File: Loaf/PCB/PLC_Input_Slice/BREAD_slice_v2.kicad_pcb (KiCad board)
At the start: 2 copper layers, 100 x 70.6 mm, 31 parts, among them J1 10018783-10200TLF, J2 Barrel_Jack, J3 DB25_Socket, U1 MCP4922-EP, U2 MCP4922-EP, U3 MCP4922-EP, U4 MCP4922-EP, U5 MCP3208, U6 MCP2561-E-P, U7 MCP2515-xSO, Y1 16MHZ Crystal

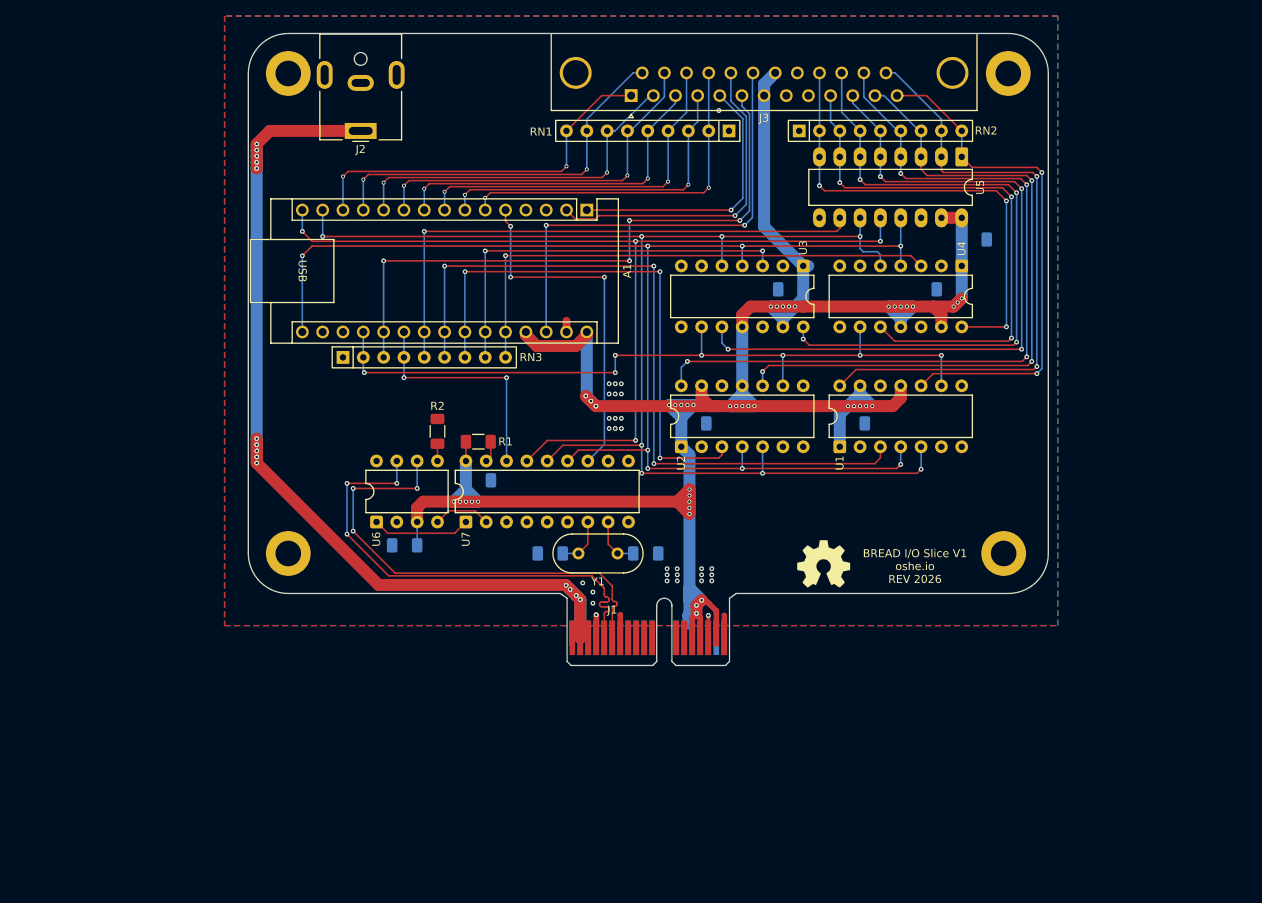
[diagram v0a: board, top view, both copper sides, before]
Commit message: IO PCB redesign progress upload
Switching to pi pico for better performance and to keep UART interface
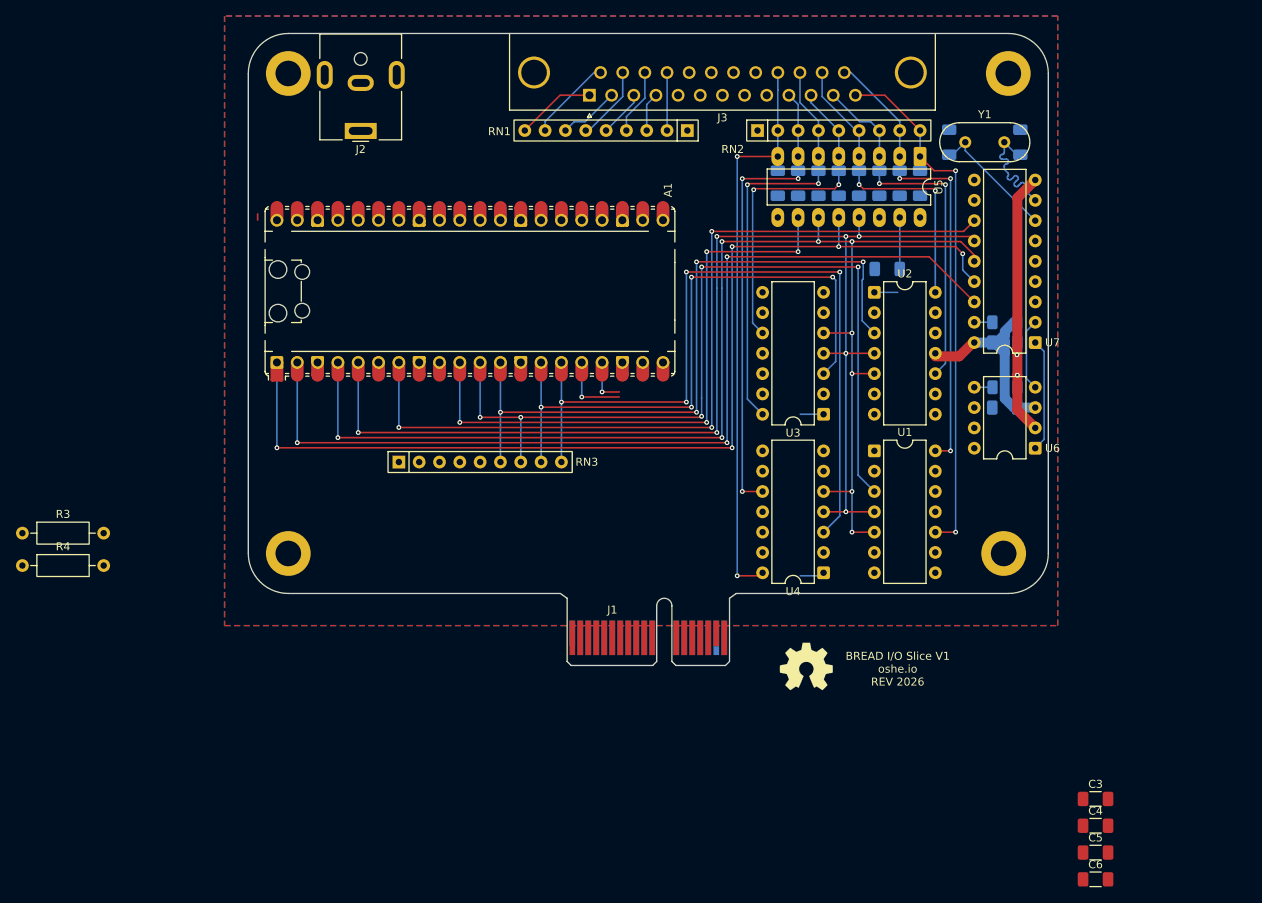
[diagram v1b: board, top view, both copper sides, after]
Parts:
- added C10: 10pF, Capacitor_SMD:C_1206_3216Metric_Pad1.33x1.80mm_HandSolder, B.Cu at (185.4, 74.2)
- added C11: 10pF, Capacitor_SMD:C_1206_3216Metric_Pad1.33x1.80mm_HandSolder, B.Cu at (182.9, 74.2)
- added C12: 10pF, Capacitor_SMD:C_1206_3216Metric_Pad1.33x1.80mm_HandSolder, B.Cu at (180.3, 74.2)
- added C13: 150pF, Capacitor_SMD:C_1206_3216Metric_Pad1.33x1.80mm_HandSolder, B.Cu at (177.8, 74.2)
- added C14: 10pF, Capacitor_SMD:C_1206_3216Metric_Pad1.33x1.80mm_HandSolder, B.Cu at (167.6, 74.2)
- added C15: 10pF, Capacitor_SMD:C_1206_3216Metric_Pad1.33x1.80mm_HandSolder, B.Cu at (170.2, 74.2)
- added C16: 10pF, Capacitor_SMD:C_1206_3216Metric_Pad1.33x1.80mm_HandSolder, B.Cu at (172.7, 74.2)
- added C17: 150pF, Capacitor_SMD:C_1206_3216Metric_Pad1.33x1.80mm_HandSolder, B.Cu at (175.3, 74.2)
- added R3: 10K, Resistor_THT:R_Axial_DIN0207_L6.3mm_D2.5mm_P10.16mm_Horizontal, F.Cu at (73.2, 118.0)
- added R4: 10K, Resistor_THT:R_Axial_DIN0207_L6.3mm_D2.5mm_P10.16mm_Horizontal, F.Cu at (73.2, 122.0)
- A1: value Arduino_Nano_Every -> RaspberryPi_Pico; footprint Module:Arduino_Nano -> Module:RaspberryPi_Pico_Common_Unspecified
- C3, C4, C5, C6: moved to F.Cu
- R1, R2: moved to B.Cu
- moved U6 82.9 mm to (199.8, 107.4), turned to 180 degrees
- moved C5 80.1 mm to (207.4, 157.9)
- moved C8 77.0 mm to (196.0, 102.3)
- moved C6 76.0 mm to (207.4, 161.3)
- moved U7 74.6 mm to (199.8, 94.2), turned to 180 degrees
- moved C1 71.6 mm to (189.1, 69.1), turned to 90 degrees
- moved R2 71.2 mm to (196.0, 99.7), turned to 180 degrees
- moved C4 71.1 mm to (207.4, 154.6), turned to 0 degrees
- moved Y1 70.6 mm to (195.9, 69.1)
- moved C2 69.5 mm to (198.0, 69.1), turned to 90 degrees
- moved C9 68.0 mm to (196.0, 94.2)
- moved R1 67.5 mm to (196.0, 91.6), turned to 0 degrees
- moved C3 55.9 mm to (207.4, 151.2), turned to 0 degrees
- moved U4 42.1 mm to (173.4, 122.9), turned to 180 degrees
- moved U2 30.9 mm to (179.7, 87.9), turned to 0 degrees
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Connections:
- A1 pad 1: /UTX -> /MISO
- A1 pad 10: /DIO3 -> /ADC1
- A1 pad 11: /DIO2 -> /DAC1
- A1 pad 12: /DIO1 -> /DAC2
- A1 pad 13: /DIO0 -> GND
- A1 pad 14: /MOSI -> /DAC3
- A1 pad 15: /MISO -> /DAC4
- A1 pad 16: /SCK -> /UTX
- A1 pad 17: +3.3V -> /URX
- A1 pad 18: unconnected-(A1-AREF-Pad18) -> GND
- A1 pad 19: /SHDN -> unconnected-(A1-GPIO14-Pad19)
- A1 pad 2: /URX -> /CAN_CS
- A1 pad 20: /ESTOP -> unconnected-(A1-GPIO15-Pad20)
- A1 pad 21: /CAN_CS -> /DIO7
- A1 pad 22: /CS1 -> /DIO6
- A1 pad 23: /DAC1 -> GND
- A1 pad 24: /DAC2 -> /DIO5
- A1 pad 25: /DAC3 -> /DIO4
- A1 pad 26: /DAC4 -> /DIO3
- A1 pad 27: +5V -> /DIO2
- A1 pad 28: /RESET -> GND
- A1 pad 29: GND -> /DIO1
- A1 pad 3: unconnected-(A1-~{RESET}-Pad3) -> GND
- A1 pad 30: +5V -> /RESET
- A1 pad 4: GND -> /MOSI
- A1 pad 5: /INT -> /SCK
- A1 pad 6: /DIO7 -> /INT
- A1 pad 7: /DIO6 -> /SHDN
- A1 pad 8: /DIO5 -> GND
- A1 pad 9: /DIO4 -> /ESTOP
- J1 pad A11: unconnected-(J1-PadA11) -> /Spare7
- J1 pad A5: unconnected-(J1-PadA5) -> /Spare5
- J1 pad A6: unconnected-(J1-PadA6) -> /Spare6
- J1 pad A7: unconnected-(J1-PadA7) -> /SCL
- J1 pad A8: unconnected-(J1-PadA8) -> /SDA
- J1 pad B10: unconnected-(J1-PadB10) -> /Spare1
- J1 pad B11: unconnected-(J1-PadB11) -> /Spare2
- J1 pad B12: unconnected-(J1-PadB12) -> /Spare3
- J1 pad B13: unconnected-(J1-PadB13) -> /Spare4
- RN3 pad 1: GND -> +5V
- RN3 pad 2: /SHDN -> unconnected-(RN3-R1-Pad2)
- RN3 pad 3: /ESTOP -> unconnected-(RN3-R2-Pad3)
- RN3 pad 6: /DAC1 -> /DAC2
- RN3 pad 7: /DAC2 -> /DAC1
- U5 pad 10: /CS1 -> /ADC1
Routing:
- net +5V: track 306.9 -> 43.7 mm, vias 44 -> 0
- net +12V: track 119.3 -> 0.00 mm, vias 14 -> 0
- net /SHDN: track 94.2 -> 0.00 mm, vias 7 -> 0
- net /CAN_CS: track 29.0 -> 120.2 mm, vias 2 -> 3
- net /ESTOP: track 78.0 -> 0.00 mm, vias 4 -> 0
- net /ADC1: track 0.00 -> 75.4 mm, vias 0 -> 4
- net /CS1: track 69.2 -> 0.00 mm, vias 1 -> 0
- net /INT: track 44.2 -> 105.1 mm
- net /AIO3: track 98.6 -> 39.1 mm, vias 4 -> 2
- net /CANL: track 59.2 -> 0.00 mm, vias 3 -> 0
- net /CANH: track 59.2 -> 0.00 mm, vias 3 -> 0
- net /RESET: track 57.6 -> 0.00 mm, vias 2 -> 0
- net /AIO4: track 89.7 -> 44.3 mm, vias 4 -> 2
- net /AIO2: track 85.5 -> 46.8 mm, vias 3 -> 2
- net /DIO1: track 47.9 -> 10.6 mm, vias 2 -> 0
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
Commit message: Finished I/O Slice redesign with pico
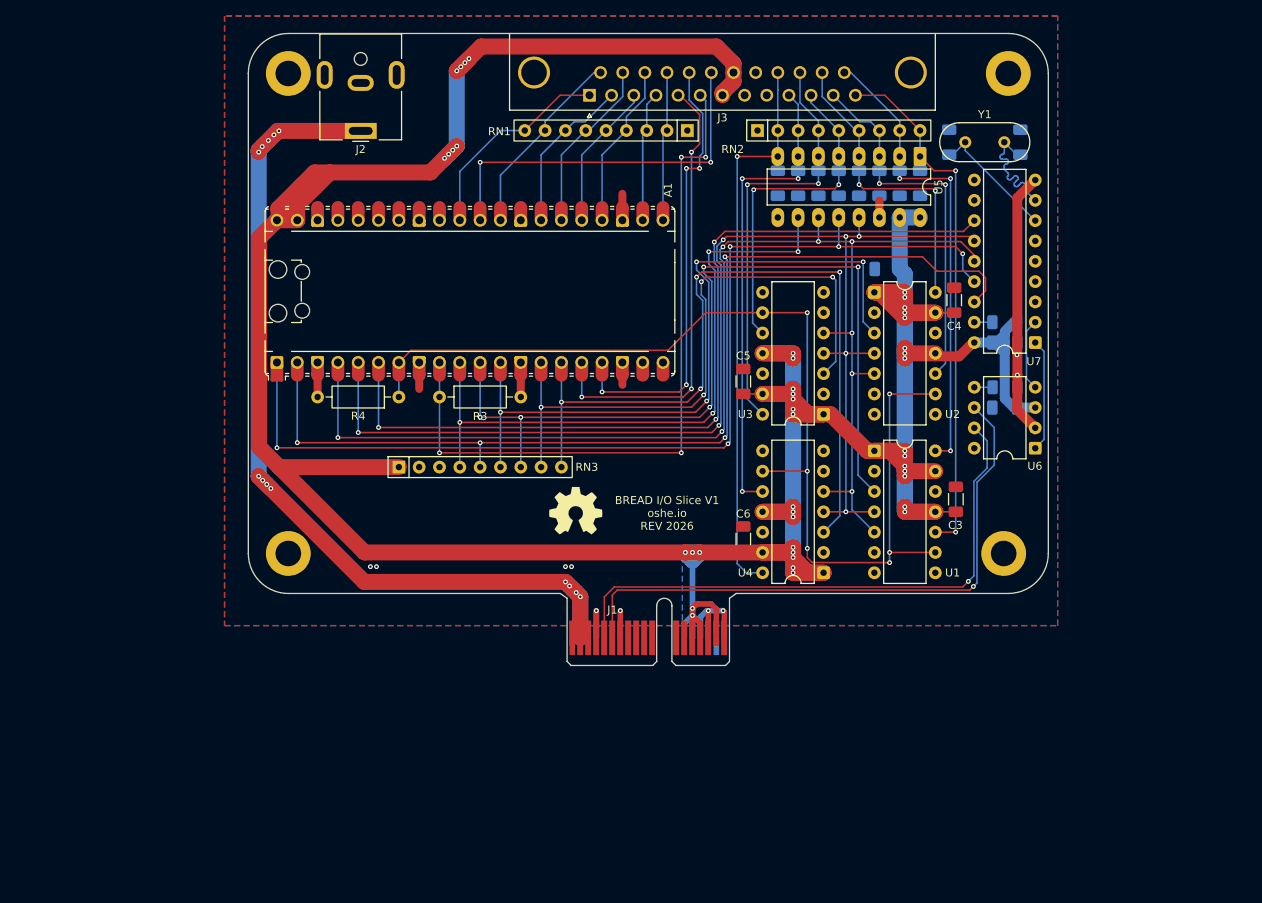
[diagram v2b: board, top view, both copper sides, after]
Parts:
- moved C5 73.5 mm to (163.3, 99.0), turned to -90 degrees
- moved C4 68.0 mm to (189.7, 88.9), turned to -90 degrees
- moved C6 61.2 mm to (163.3, 118.7), turned to -90 degrees
- moved R3 54.8 mm to (125.3, 101.0)
- moved R4 51.6 mm to (120.3, 101.0), turned to 180 degrees
- moved C3 41.3 mm to (189.9, 113.8), turned to -90 degrees
- moved Logo1 34.8 mm to (142.4, 115.2)
- moved RN3 0.63 mm to (120.3, 109.7)
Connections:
- RN3 pad 4: /CAN_CS -> /ADC1
- RN3 pad 5: /CS1 -> /CAN_CS
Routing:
- net +5V: track 43.7 -> 542.5 mm, vias 0 -> 43
- net /SHDN: track 0.00 -> 137.2 mm, vias 0 -> 6
- net +12V: track 0.00 -> 119.8 mm, vias 0 -> 13
- net /ESTOP: track 0.00 -> 89.6 mm, vias 0 -> 4
- net /CANL: track 0.00 -> 75.4 mm, vias 0 -> 1
- net /CANH: track 0.00 -> 72.2 mm, vias 0 -> 1
- net /URX: track 5.84 -> 56.1 mm, vias 1 -> 4
- net /UTX: track 9.02 -> 57.2 mm, vias 1 -> 3
- net /RESET: track 0.00 -> 47.3 mm, vias 0 -> 2
- net GND: track 35.8 -> 79.2 mm, vias 2 -> 10
- net /DIO0: track 9.91 -> 26.2 mm
- net /DIO1: track 10.6 -> 24.1 mm
- net /DIO5: track 8.20 -> 20.7 mm
- net /DIO2: track 7.60 -> 20.1 mm
- net /DIO4: track 5.84 -> 18.3 mm
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- added copper zone on B.Cu, net +5V

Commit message: Updated DRC to fit new OSHE specs
pain
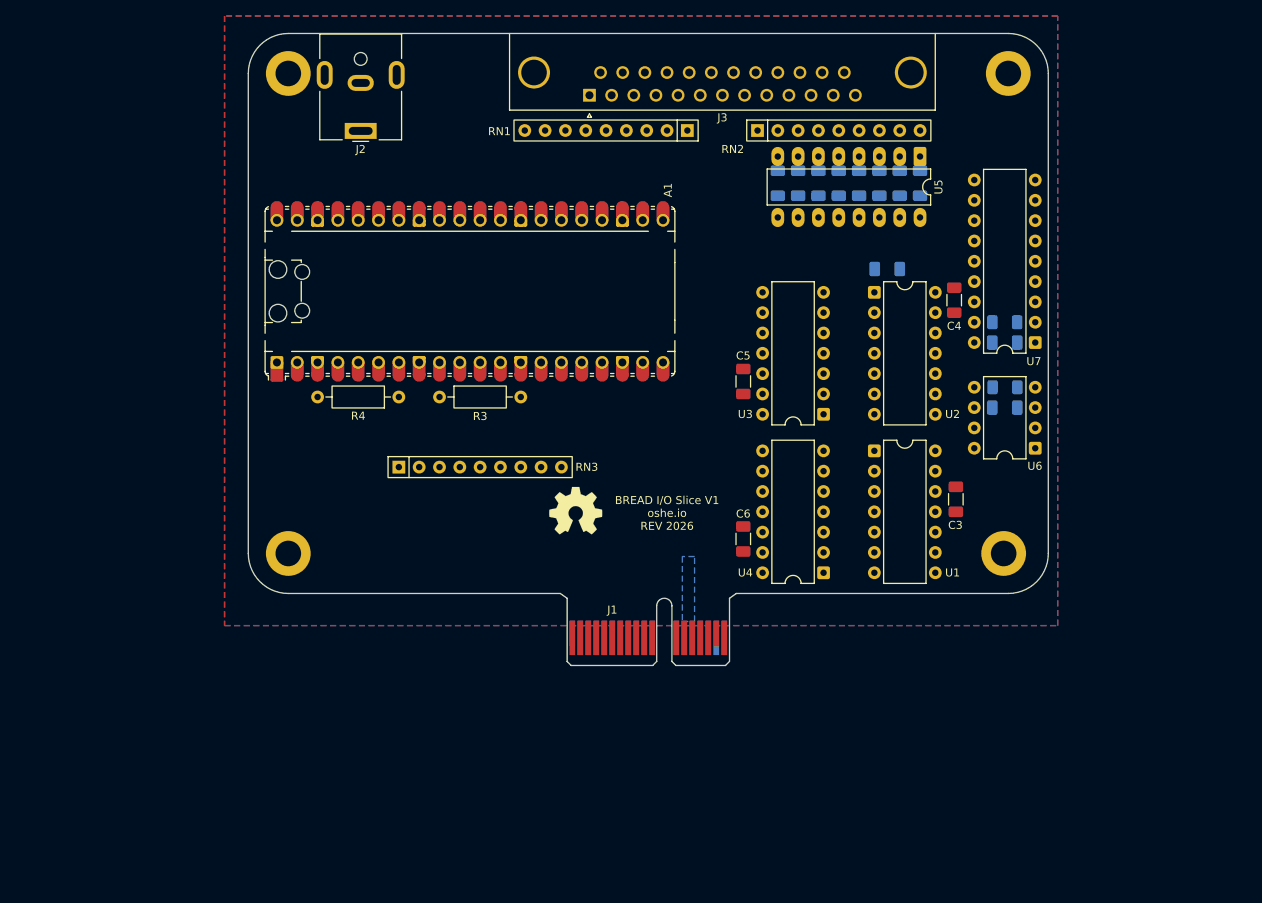
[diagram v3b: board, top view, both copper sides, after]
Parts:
- removed C1, C2: 20pf, Capacitor_SMD:C_1206_3216Metric_Pad1.33x1.80mm_HandSolder
- removed Y1: 16MHZ Crystal, Crystal:Crystal_HC49-4H_Vertical
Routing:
- net +5V: track 542.5 -> 0.00 mm, vias 43 -> 0
- net /MOSI: track 165.2 -> 0.00 mm, vias 8 -> 0
- net /SCK: track 159.7 -> 0.00 mm, vias 7 -> 0
- net /SHDN: track 137.2 -> 0.00 mm, vias 6 -> 0
- net /MISO: track 129.2 -> 0.00 mm, vias 5 -> 0
- net /CAN_CS: track 126.9 -> 0.00 mm, vias 4 -> 0
- net +12V: track 119.8 -> 0.00 mm, vias 13 -> 0
- net /DAC1: track 108.6 -> 0.00 mm, vias 5 -> 0
- net /INT: track 106.8 -> 0.00 mm, vias 3 -> 0
- net /DAC4: track 97.1 -> 0.00 mm, vias 4 -> 0
- net /ESTOP: track 89.6 -> 0.00 mm, vias 4 -> 0
- net /DAC2: track 87.9 -> 0.00 mm, vias 4 -> 0
- net /ADC1: track 81.2 -> 0.00 mm, vias 4 -> 0
- net GND: track 79.2 -> 0.00 mm, vias 10 -> 0
- net /DAC3: track 78.2 -> 0.00 mm, vias 4 -> 0
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
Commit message: Work on new new new new IO Slice
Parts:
- removed R3, R4: 10K, Resistor_THT:R_Axial_DIN0207_L6.3mm_D2.5mm_P10.16mm_Horizontal
- added C1: 20pf, Capacitor_SMD:C_1206_3216Metric_Pad1.33x1.80mm_HandSolder, F.Cu at (216.9, 71.1)
- added C2: 20pf, Capacitor_SMD:C_1206_3216Metric_Pad1.33x1.80mm_HandSolder, F.Cu at (216.9, 74.5)
- added Y1: 16MHZ Crystal, Crystal:Crystal_HC49-4H_Vertical, F.Cu at (218.0, 66.1)
- C3, C4, C5, C6: moved to B.Cu
- C7: moved to F.Cu
- moved C7 10.6 mm to (188.2, 76.9), turned to -90 degrees
- moved C3 9.42 mm to (181.6, 109.3), turned to 90 degrees
- moved C6 9.28 mm to (172.2, 121.4)
- moved C5 9.25 mm to (172.2, 101.6)
- moved RN3 8.76 mm to (120.3, 101.0)
- moved C4 7.97 mm to (181.7, 89.4), turned to 90 degrees
- moved U1 0.89 mm to (174.2, 122.9)
- moved U2 0.89 mm to (174.2, 103.1)
- renumbered U4 to U1, U3 to U2, U2 to U3, U1 to U4
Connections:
- A1 pad 11: /DAC1 -> /DAC4
- A1 pad 12: /DAC2 -> /DAC3
- A1 pad 14: /DAC3 -> /DAC2
- A1 pad 15: /DAC4 -> /DAC1
- A1 pad 7: /SHDN -> /ESTOP
- A1 pad 9: /ESTOP -> /SHDN
- RN3 pad 1: +5V -> GND
- RN3 pad 2: unconnected-(RN3-R1-Pad2) -> /ESTOP
- RN3 pad 3: unconnected-(RN3-R2-Pad3) -> /SHDN
- RN3 pad 5: /CAN_CS -> /DAC4
- RN3 pad 6: /DAC2 -> /DAC3
- RN3 pad 7: /DAC1 -> /CAN_CS
- RN3 pad 8: /DAC3 -> /DAC2
- RN3 pad 9: /DAC4 -> /DAC1
- U1 pad 10: /AIO6 -> /AIO5
- U1 pad 14: /AIO7 -> /AIO4
- U1 pad 3: /DAC4 -> /DAC1
- U2 pad 10: /AIO4 -> /AIO7
- U2 pad 14: /AIO5 -> /AIO6
- U2 pad 3: /DAC3 -> /DAC2
- U3 pad 10: /AIO2 -> /AIO1
- U3 pad 14: /AIO3 -> /AIO0
- U3 pad 3: /DAC2 -> /DAC3
- U4 pad 10: /AIO0 -> /AIO3
- U4 pad 14: /AIO1 -> /AIO2
- U4 pad 3: /DAC1 -> /DAC4
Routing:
- net +5V: track 0.00 -> 152.6 mm, vias 0 -> 17
- net /AIO4: track 0.00 -> 75.8 mm, vias 0 -> 2
- net /AIO5: track 0.00 -> 65.9 mm, vias 0 -> 4
- net /AIO6: track 0.00 -> 51.3 mm, vias 0 -> 4
- net /AIO3: track 0.00 -> 46.9 mm
- net /MOSI: track 0.00 -> 42.7 mm, vias 0 -> 4
- net /SCK: track 0.00 -> 41.5 mm, vias 0 -> 2
- net /AIO7: track 0.00 -> 40.0 mm, vias 0 -> 3
- net /DAC1: track 0.00 -> 35.6 mm
- net /AIO2: track 0.00 -> 34.8 mm
- net /DAC4: track 0.00 -> 30.6 mm
- net /AIO1: track 0.00 -> 28.2 mm
- net /AIO0: track 0.00 -> 17.0 mm
- net /DAC2: track 0.00 -> 16.0 mm
- net /DAC3: track 0.00 -> 11.7 mm
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- removed copper zone on B.Cu, net +5V
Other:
- board text added: "U3"
- board text added: "U4"

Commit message: I/O Slice Updated
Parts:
- C7: moved to B.Cu
- moved C1 24.5 mm to (193.0, 65.3)
- moved RN1 22.9 mm to (133.5, 67.7), turned to 0 degrees
- moved RN2 22.9 mm to (188.0, 67.7), turned to 180 degrees
- moved C2 20.9 mm to (198.1, 65.3), turned to 180 degrees
- moved Y1 20.1 mm to (198.1, 69.3), turned to 180 degrees
- moved C7 6.32 mm to (185.4, 82.6), turned to 90 degrees
- moved A1 0.51 mm to (129.7, 87.7)
- moved RN3 0.51 mm to (120.8, 101.0)
- moved C13 0.39 mm to (177.8, 74.6)
- moved C10 0.39 mm to (185.4, 74.6)
- moved C11 0.39 mm to (182.9, 74.6)
- moved C12 0.39 mm to (180.3, 74.6)
- moved C14 0.39 mm to (167.6, 74.6)
- moved C15 0.39 mm to (170.2, 74.6)
- moved C16 0.39 mm to (172.7, 74.6)
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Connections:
- A1 pad 20: unconnected-(A1-GPIO15-Pad20) -> /Sl1Lt
- J3 pad 18: /URX -> /UTX
- J3 pad 5: /UTX -> /URX
- RN1 pad 2: /DIO7 -> /DIO0
- RN1 pad 3: /DIO6 -> /DIO1
- RN1 pad 4: /DIO5 -> /DIO2
- RN1 pad 5: /DIO4 -> /DIO3
- RN1 pad 6: /DIO3 -> /DIO4
- RN1 pad 7: /DIO2 -> /DIO5
- RN1 pad 8: /DIO1 -> /DIO6
- RN1 pad 9: /DIO0 -> /DIO7
- RN2 pad 2: /AIO7 -> /AIO0
- RN2 pad 3: /AIO6 -> /AIO1
- RN2 pad 4: /AIO5 -> /AIO2
- RN2 pad 5: /AIO4 -> /AIO3
- RN2 pad 6: /AIO3 -> /AIO4
- RN2 pad 7: /AIO2 -> /AIO5
- RN2 pad 8: /AIO1 -> /AIO6
- RN2 pad 9: /AIO0 -> /AIO7
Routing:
- net +5V: track 152.6 -> 402.5 mm, vias 17 -> 24
- net +12V: track 0.00 -> 140.5 mm, vias 0 -> 18
- net /MISO: track 0.00 -> 125.7 mm, vias 0 -> 4
- net /MOSI: track 42.7 -> 166.7 mm, vias 4 -> 9
- net /SCK: track 41.5 -> 160.4 mm, vias 2 -> 6
- net /CAN_CS: track 0.00 -> 115.3 mm, vias 0 -> 3
- net /SHDN: track 4.32 -> 112.8 mm, vias 0 -> 4
- net /INT: track 0.66 -> 108.6 mm, vias 0 -> 3
- net /ESTOP: track 4.57 -> 85.6 mm, vias 0 -> 2
- net /CANL: track 0.00 -> 72.4 mm, vias 0 -> 1
- net /CANH: track 0.00 -> 72.4 mm, vias 0 -> 1
- net /DAC4: track 30.6 -> 101.1 mm, vias 0 -> 4
- net /DAC3: track 11.7 -> 80.9 mm, vias 0 -> 4
- net /ADC1: track 8.99 -> 73.0 mm, vias 0 -> 3
- net /UTX: track 0.00 -> 56.9 mm, vias 0 -> 2
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
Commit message: Redid io gerbers
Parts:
- added F1: Polyfuse, Fuse:Fuse_2920_7451Metric_Pad2.10x5.45mm_HandSolder, B.Cu at (106.2, 66.9)
- C10, C11, C12, C14, C15, C16: value 10pF -> 150pF
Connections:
- J2 pad 1: +12V -> 12VO
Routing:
- net +12V: track 140.5 -> 123.7 mm, vias 18 -> 12
- net 12VO: track 0.00 -> 6.13 mm
- net GND: vias 24 -> 20
